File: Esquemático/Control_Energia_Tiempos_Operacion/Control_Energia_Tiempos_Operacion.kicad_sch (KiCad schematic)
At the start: 9 parts, among them Q1 BC548, U1 ATmega328P-P, U2 DS3231M

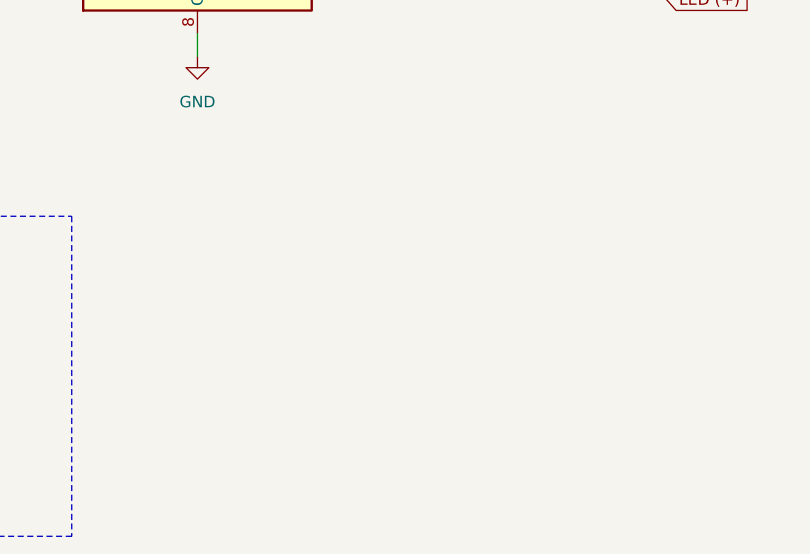
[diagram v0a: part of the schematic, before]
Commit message: ERC completo en esquemático
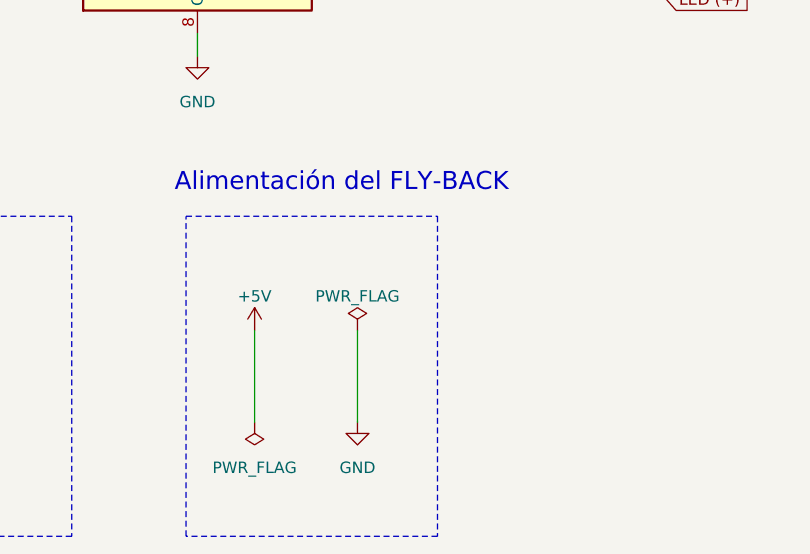
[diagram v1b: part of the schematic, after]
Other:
- note added: "Alimentación del FLY-BACK"
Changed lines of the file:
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@@
+    (stroke (width 0) (type default))
+  )
+  (wire (pts (xy 144.78 160.02) (xy 144.78 170.18))
     (stroke (width 0) (type default))
   )
@@
   )
   (wire (pts (xy 170.18 63.5) (xy 172.72 63.5))
+    (stroke (width 0) (type default))
+  )
+  (wire (pts (xy 156.21 160.02) (xy 156.21 170.18))
     (stroke (width 0) (type default))
   )
@@
     (fill (type none))
   )
+  (rectangle (start 137.16 147.32) (end 165.1 182.88)
+    (stroke (width 0) (type dash))
+    (fill (type none))
+  )
   (rectangle (start 209.55 54.61) (end 281.94 129.54)
     (stroke (width 0) (type dash))
     (fill (type none))
+  )
+  (text "Alimentación del FLY-BACK" (at 135.89 144.78 0)
+    (effects (font (face "Times New Roman") (size 2 2)) (justify left bottom))
   )
   (text "LCD 16x2	" (at 236.22 50.8 0)
@@
         (path "/29f28840-be5d-439f-bf59-d6cd8302648e"
           (reference "#PWR08") (unit 1)
+        )
+      )
+    )
+  )
+  (symbol (lib_id "power:GND") (at 156.21 170.18 0) (unit 1)
+    (in_bom yes) (on_board yes) (dnp no) (fields_autoplaced)
+    (property "Reference" "#PWR019" (at 156.21 176.53 0)
+      (effects (font (size 1.27 1.27)) hide)
+    )
+    (property "Value" "GND" (at 156.21 175.26 0)
+      (effects (font (size 1.27 1.27)))
+    )
+    (property "Footprint" "" (at 156.21 170.18 0)
+      (effects (font (size 1.27 1.27)) hide)
+    )
+    (property "Datasheet" "" (at 156.21 170.18 0)
+      (effects (font (size 1.27 1.27)) hide)
+    )
+    (pin "1")
+    (instances
+      (project "Control_Energia_Tiempos_Operacion"
+        (path "/29f28840-be5d-439f-bf59-d6cd8302648e"
+          (reference "#PWR019") (unit 1)
         )
       )
@@
     )
   )
+  (symbol (lib_id "power:+5V") (at 144.78 160.02 0) (unit 1)
+    (in_bom yes) (on_board yes) (dnp no) (fields_autoplaced)
+    (property "Reference" "#PWR018" (at 144.78 163.83 0)
+      (effects (font (size 1.27 1.27)) hide)
+    )
+    (property "Value" "+5V" (at 144.78 156.21 0)
+      (effects (font (size 1.27 1.27)))
+    )
+    (property "Footprint" "" (at 144.78 160.02 0)
+      (effects (font (size 1.27 1.27)) hide)
+    )
+    (property "Datasheet" "" (at 144.78 160.02 0)
+      (effects (font (size 1.27 1.27)) hide)
+    )
+    (pin "1")
+    (instances
+      (project "Control_Energia_Tiempos_Operacion"
+        (path "/29f28840-be5d-439f-bf59-d6cd8302648e"
+          (reference "#PWR018") (unit 1)
+        )
+      )
+    )
+  )
   (symbol (lib_id "power:+5V") (at 182.88 102.87 0) (unit 1)
     (in_bom yes) (on_board yes) (dnp no) (fields_autoplaced)
@@
         (path "/29f28840-be5d-439f-bf59-d6cd8302648e"
           (reference "#PWR03") (unit 1)
+        )
+      )
+    )
+  )
+  (symbol (lib_id "power:PWR_FLAG") (at 144.78 170.18 180) (unit 1)
+    (in_bom yes) (on_board yes) (dnp no) (fields_autoplaced)
+    (property "Reference" "#FLG01" (at 144.78 172.085 0)
+      (effects (font (size 1.27 1.27)) hide)
+    )
+    (property "Value" "PWR_FLAG" (at 144.78 175.26 0)
+      (effects (font (size 1.27 1.27)))
+    )
+    (property "Footprint" "" (at 144.78 170.18 0)
+      (effects (font (size 1.27 1.27)) hide)
+    )
+    (property "Datasheet" "~" (at 144.78 170.18 0)
+      (effects (font (size 1.27 1.27)) hide)
+    )
+    (pin "1")
+    (instances
+      (project "Control_Energia_Tiempos_Operacion"
+        (path "/29f28840-be5d-439f-bf59-d6cd8302648e"
+          (reference "#FLG01") (unit 1)
         )
       )
@@
         )
       )
+    )
+  )
+  (symbol (lib_id "power:PWR_FLAG") (at 156.21 160.02 0) (unit 1)
+    (in_bom yes) (on_board yes) (dnp no) (fields_autoplaced)
+    (property "Reference" "#FLG02" (at 156.21 158.115 0)
+      (effects (font (size 1.27 1.27)) hide)
+    )
+    (property "Value" "PWR_FLAG" (at 156.21 156.21 0)
+      (effects (font (size 1.27 1.27)))
+    )
+    (property "Footprint" "" (at 156.21 160.02 0)
+      (effects (font (size 1.27 1.27)) hide)
+    )
+    (property "Datasheet" "~" (at 156.21 160.02 0)
+      (effects (font (size 1.27 1.27)) hide)
+    )
+    (pin "1")
+    (instances
+      (project "Control_Energia_Tiempos_Operacion"
+        (path "/29f28840-be5d-439f-bf59-d6cd8302648e"
+          (reference "#FLG02") (unit 1)
+        )
+      )

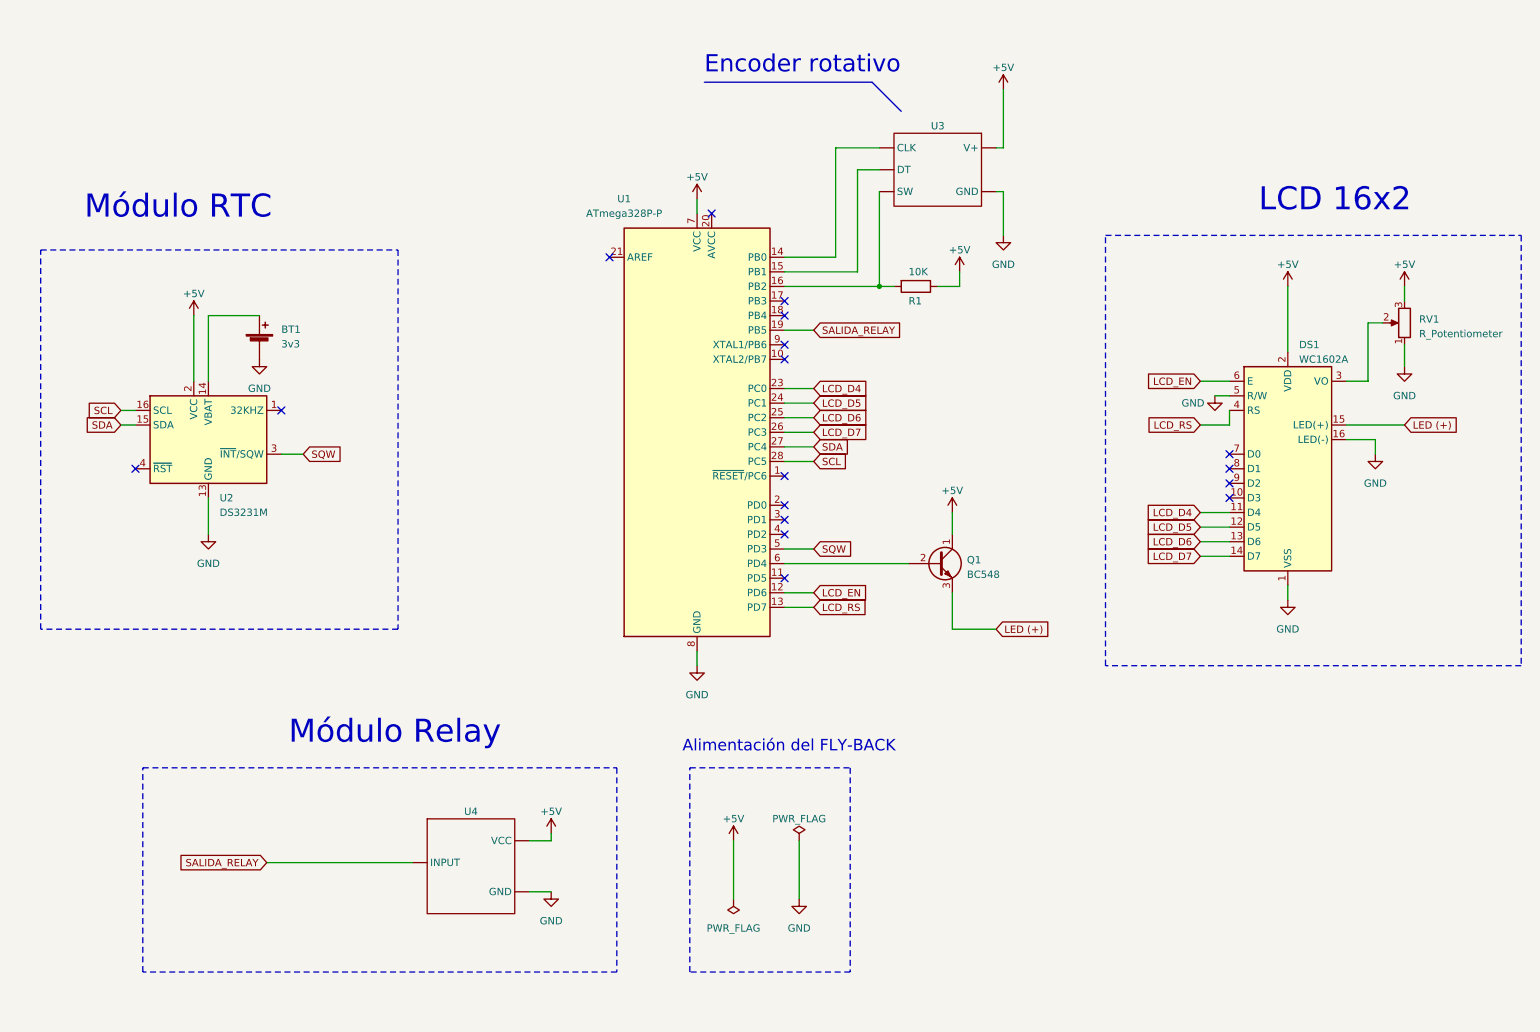
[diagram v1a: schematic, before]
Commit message: Esquemático y PCBs actualizado, incluye uSD
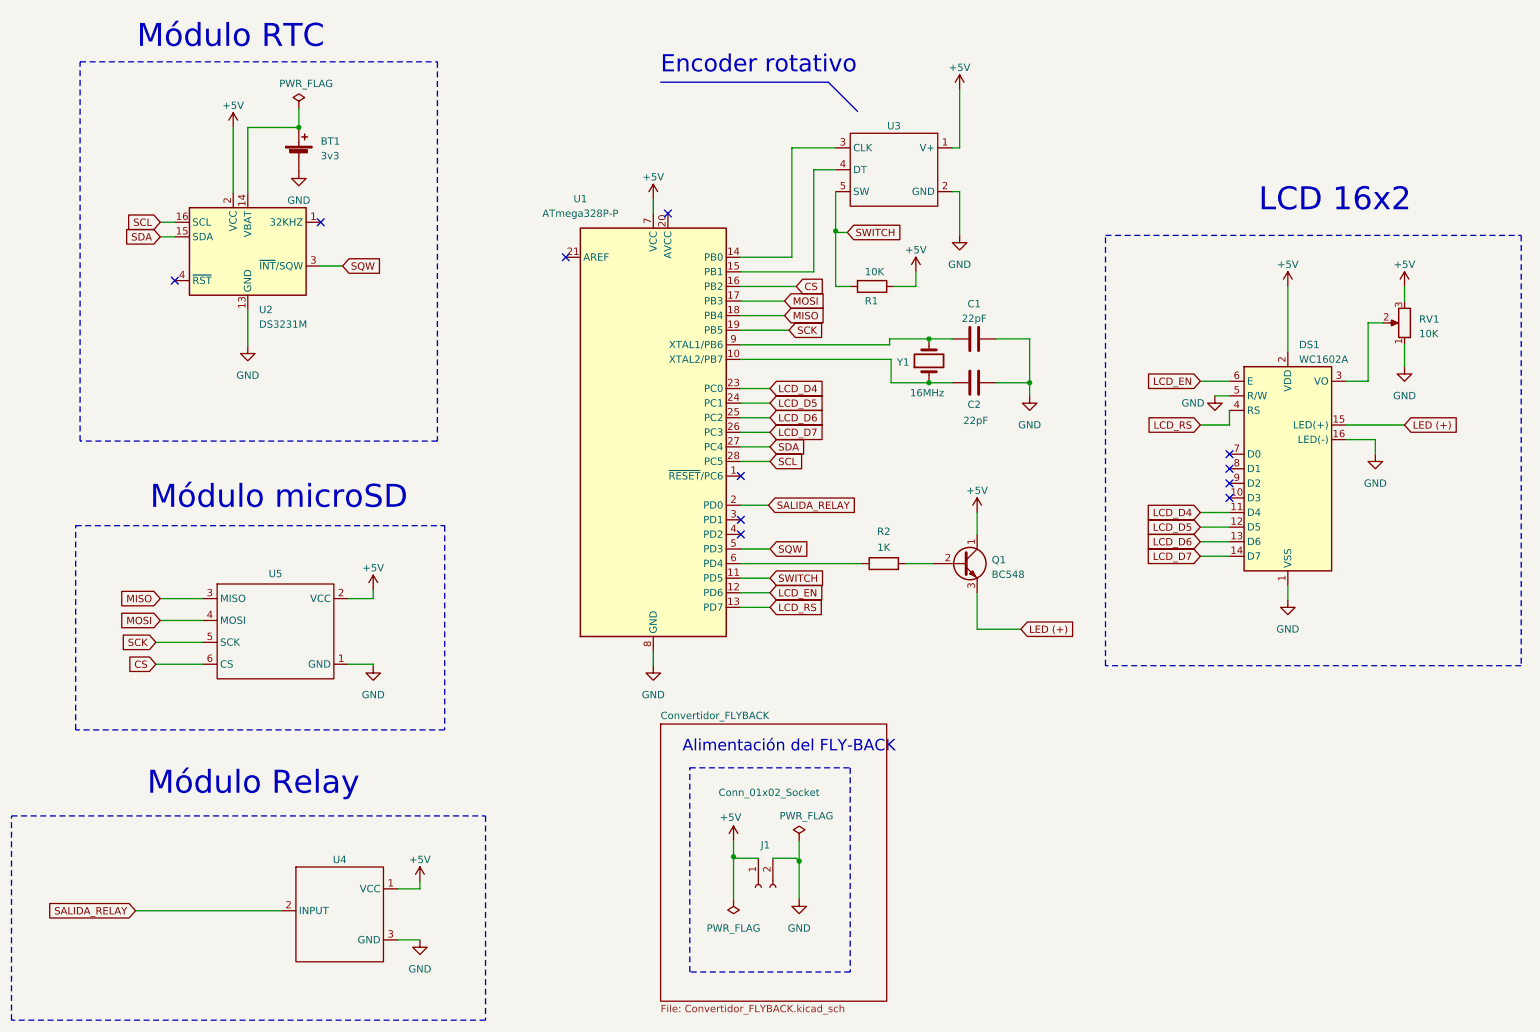
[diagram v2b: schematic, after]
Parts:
- added C1, C2: 22pF, Capacitor_THT:C_Disc_D5.0mm_W2.5mm_P2.50mm, symbol Device:C
- added J1: Conn_01x02_Socket, TerminalBlock:TerminalBlock_bornier-2_P5.08mm, symbol Connector:Conn_01x02_Socket
- added R2: 1K, Resistor_THT:R_Axial_DIN0207_L6.3mm_D2.5mm_P10.16mm_Horizontal, symbol Device:R
- added U5: ~, Connector_PinSocket_2.00mm:PinSocket_1x06_P2.00mm_Vertical, symbol Modulo_uSD:Modulo_uSD
- added Y1: 16MHz, Crystal:Crystal_HC49-4H_Vertical, symbol Device:Crystal
- DS1: footprint Display:WC1602A -> Connector_IDC:IDC-Header_2x06-1MP_P2.54mm_Latch6.5mm_Vertical
- R1: footprint (none) -> Resistor_THT:R_Axial_DIN0207_L6.3mm_D2.5mm_P10.16mm_Horizontal
- RV1: value R_Potentiometer -> 10K; footprint (none) -> Potentiometer_THT:Potentiometer_Bourns_3296W_Vertical
- U2: footprint Package_SO:SOIC-16W_7.5x10.3mm_P1.27mm -> Connector_PinSocket_2.00mm:PinSocket_2x04_P2.00mm_Vertical
- U3: footprint (none) -> Connector_IDC:IDC-Header_2x03_P2.54mm_Vertical
- U4: footprint (none) -> Connector_PinSocket_2.00mm:PinSocket_1x03_P2.00mm_Vertical
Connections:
- net +5V: now also U3.1 (V+), U4.1 (VCC), J1.1 (Pin_1), U5.2 (VCC); no longer U3. (V+), U4. (VCC)
- net GND: now also U3.2 (GND), U4.3 (GND), C1.2, C2.2, J1.2 (Pin_2), U5.1 (GND); no longer U3. (V+), U4. (VCC)
- net SALIDA_RELAY: now also U1.2 (PD0), U4.2 (INPUT); no longer U1.19 (PB5), U4. (VCC)
- net at U1.10 (XTAL2/PB7): now also C2.1, Y1.1
- net SWITCH: now reaches U1.11 (PD5)
- net SWITCH: now also R1.2, U3.5 (SW)
- net at U1.14 (PB0): now also U3.3 (CLK); no longer U3. (V+)
- net at U1.15 (PB1): now also U3.4 (DT); no longer U3. (V+)
- net MOSI: now reaches U1.17 (PB3)
- net MOSI: now also U5.4 (MOSI)
- net MISO: now reaches U1.18 (PB4)
- net MISO: now also U5.3 (MISO)
- net at U1.6 (PD4): now also R2.1; no longer Q1.2 (B)
- net at U1.9 (XTAL1/PB6): now also C1.1, Y1.2
- new net: Q1.2 (B), R2.2
- new net CS: U1.16 (PB2), U5.6 (CS)
- new net SCK: U1.19 (PB5), U5.5 (SCK)
- no-connect marks 17 -> 11
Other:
- added sheet Convertidor_FLYBACK (Convertidor_FLYBACK.kicad_sch)
- note added: "Módulo microSD"
- moved on the sheet: BT1, Q1, R1, U1, U2

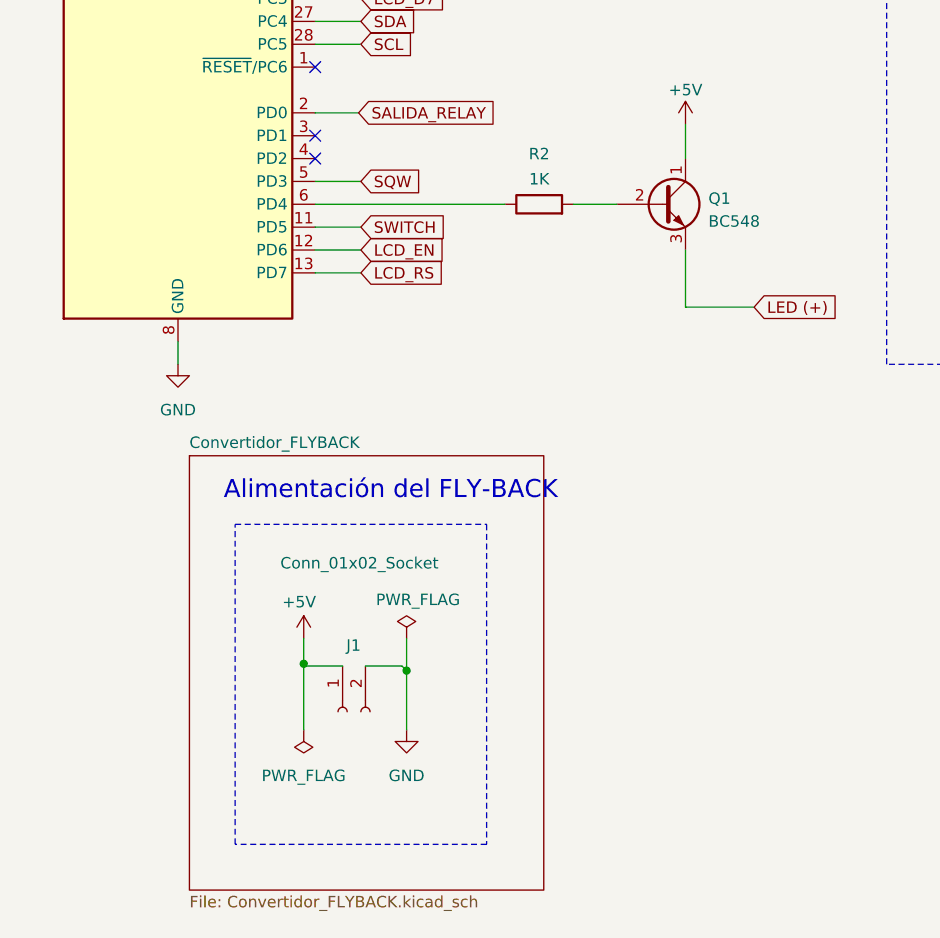
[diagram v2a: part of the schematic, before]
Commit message: Actualización de PCB, se pueden corregir algunas huellas para el armado de futuros prototipos.
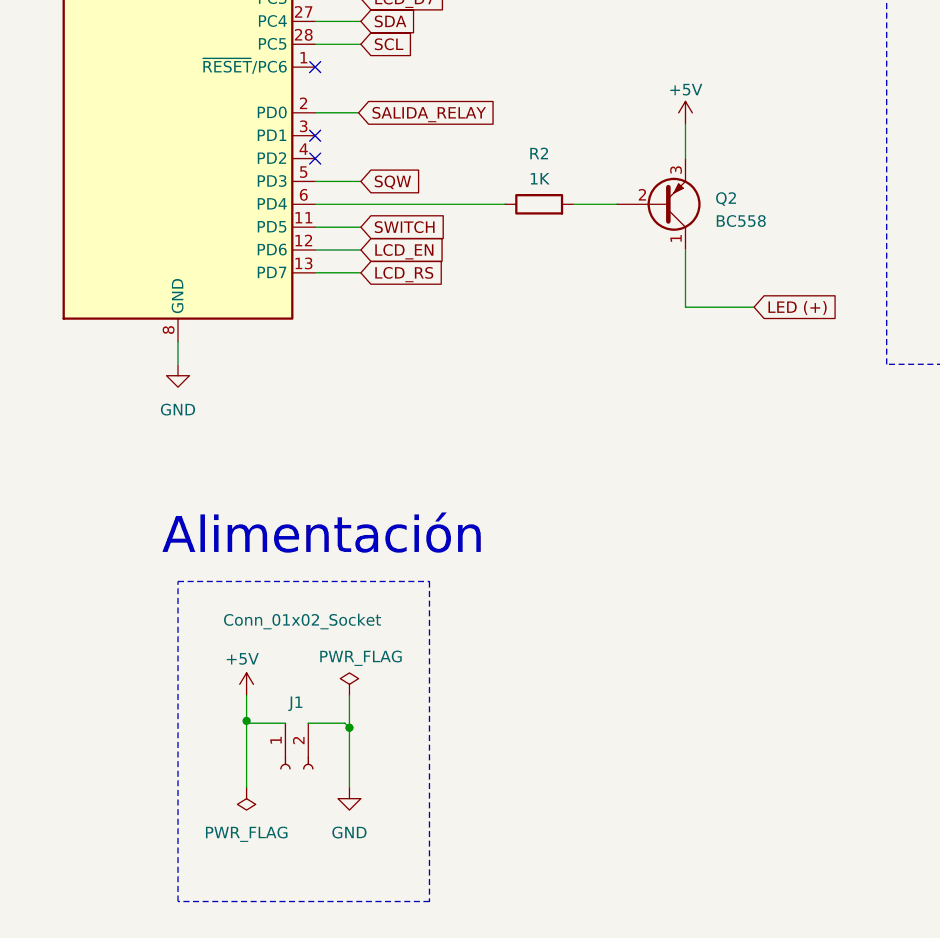
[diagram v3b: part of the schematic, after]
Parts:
- removed Q1: BC548, Package_TO_SOT_THT:TO-92_Inline, symbol Transistor_BJT:BC548
- added Q2: BC558, Package_TO_SOT_THT:TO-92_Inline, symbol Transistor_BJT:BC558
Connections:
- net +5V: now also Q2.3 (E)
- net LED (+): now also Q2.1 (C)
- net at R2.2: now also Q2.2 (B)
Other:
- removed sheet Convertidor_FLYBACK
- note added: "Alimentación"
- note removed: "Alimentación del FLY-BACK"
- moved on the sheet: J1
